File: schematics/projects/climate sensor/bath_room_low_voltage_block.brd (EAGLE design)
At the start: 100 x 80 mm, 8 parts

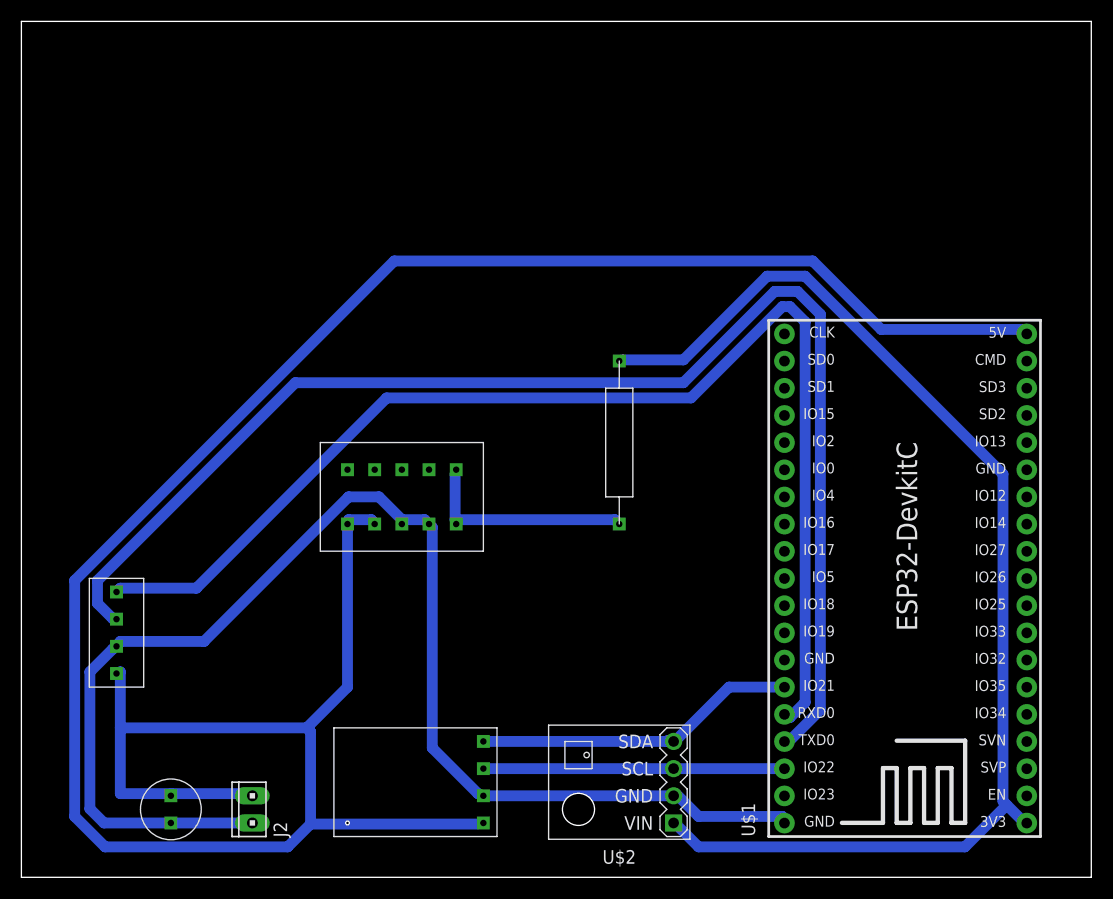
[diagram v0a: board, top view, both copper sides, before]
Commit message: added eagle board files for low-voltage schemas
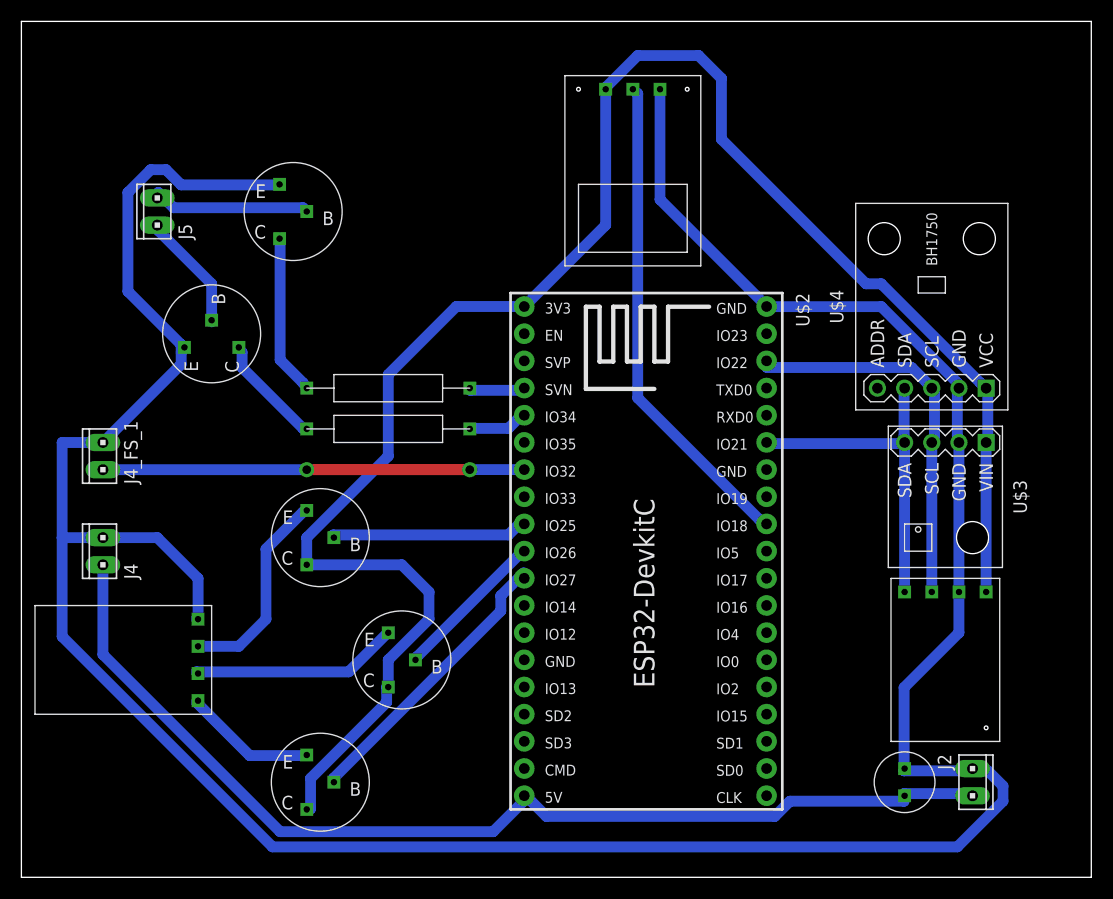
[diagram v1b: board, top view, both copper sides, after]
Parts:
- removed GY_SGP1: GY-SGP30, my_devices:GY-SGP30
- removed R1: 600, my_devices:R
- removed U$1: ESP32DEVKITC, ESP32-DEVKITC:ESP32-DEVKITC
- removed U$11: MH_Z19B, my_devices:MH_Z19B
- added GY_SGP30_1: GY-SGP30, my_devices:GY-SGP30
- added J4, J4_FS_1, J5: (no value), con-amp:10X02MTA
- added Q1, Q2, Q3, Q4, Q5: KT3102BM, my_devices:TRANSISTOR_NPN
- added R2, R3: 600, my_devices:R
- added U$4: LIGHT-SENSOR-BH1750, diy-modules:LIGHT-SENSOR-BH1750
- added U$5: TTP223, my_devices:TTP223
- added U$6: RGBLED, my_devices:RGBLED
- U$2: value TEMP-HUM-PRES-BME280 -> ESP32DEVKITC; device diy-modules:TEMP-HUM-PRES-BME280 -> ESP32-DEVKITC:ESP32-DEVKITC
- U$3: value PMS7003 -> TEMP-HUM-PRES-BME280; device my_devices:PMS7003 -> diy-modules:TEMP-HUM-PRES-BME280
- moved C1 68.6 mm to (82.5, 8.89), turned to 90 degrees
- moved J2 67.4 mm to (88.9, 8.89), turned to 270 degrees
- moved U$3 50.8 mm to (86.4, 35.6), turned to 270 degrees
- moved U$2 21.7 mm to (58.4, 30.5), turned to 270 degrees
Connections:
- removed net UART_0_RXD: U$1.34, U$11.TX
- removed net UART_0_TXD: U$1.35, U$11.RX
- removed net UART_1_RXD: U$3.TXD
- removed net UART_1_TXD: U$3.RXD
- new net GPIO_AN_A: R2.P$2, U$2.4
- new net GPIO_AN_B: R3.P$2, U$2.5
- new net GPIO_RGB_B: Q3.B, U$2.11
- new net GPIO_RGB_G: Q2.B, U$2.10
- new net GPIO_RGB_R: Q1.B, U$2.9
- new net GPIO_TTP223: U$2.30, U$5.OUT
- new net N$1: J4_FS_1.2, U$2.7
- new net N$2: Q3.E, U$6.VIN_B
- new net N$3: Q2.E, U$6.VIN_G
- new net N$4: Q1.E, U$6.VIN_R
- new net N$5: J5.1, Q5.B
- new net N$6: J5.2, Q4.B
- new net N$7: Q5.C, R2.P$1
- net +5V: now also J4.2, U$2.19; no longer U$1.19, U$11.VCC, U$3.VIN, U$3.VIN_1
- net 3V3: now also GY_SGP30_1.VIN, Q1.C, Q2.C, Q3.C, U$3.1, U$4.1, U$5.VIN; no longer GY_SGP1.VIN, R1.P$1, U$1.1
- net GND: now also GY_SGP30_1.GND, J4.1, J4_FS_1.1, Q4.E, Q5.E, U$2.38, U$3.2, U$4.2, U$5.GND, U$6.GND; no longer GY_SGP1.GND, U$1.38, U$11.GND, U$2.2, U$3.GND, U$3.GND_1
- net I2C_SCL: now also GY_SGP30_1.SCL, U$2.36, U$3.3, U$4.3; no longer GY_SGP1.SCL, U$1.36, U$2.3
- net I2C_SDA: now also GY_SGP30_1.SDA, U$2.33, U$3.4, U$4.4; no longer GY_SGP1.SDA, U$1.33, U$2.4
- net N$8: now also Q4.C, R3.P$1; no longer R1.P$2, U$3.RESET, U$3.SET
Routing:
- net GND: track 125.7 -> 278.8 mm
- net +5V: track 241.8 -> 100.4 mm
- net UART_0_TXD: track 125.7 -> 0.00 mm
- net UART_0_RXD: track 114.2 -> 0.00 mm
- net 3V3: track 114.2 -> 170.0 mm
- net GPIO_TTP223: track 0.00 -> 45.9 mm
- net N$1: track 0.00 -> 39.4 mm, vias 0 -> 2
- net GPIO_RGB_B: track 0.00 -> 27.4 mm
- net N$3: track 0.00 -> 19.7 mm
- net N$4: track 0.00 -> 19.2 mm
- net GPIO_RGB_R: track 0.00 -> 19.0 mm
- net N$5: track 0.00 -> 15.1 mm
- net N$7: track 0.00 -> 15.1 mm
- net GPIO_RGB_G: track 0.00 -> 14.5 mm
- net N$2: track 0.00 -> 12.6 mm
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
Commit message: changes in board files.
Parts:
- moved Q5 1.27 mm to (25.4, 63.5)
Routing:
- net GND: track 278.8 -> 303.3 mm
- net +5V: track 100.4 -> 102.3 mm
- net N$7: track 15.1 -> 16.4 mm
- net N$5: track 15.1 -> 14.0 mm
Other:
- board text added: "A B"
- board text added: "AN_OUT"
- board text added: "AN_POWER"
- board text added: "FS"
- board text added: "GND +5V"
- board text added: "GND 3V3"
- board text added: "SUPPLY"
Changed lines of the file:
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@@
 <wire x1="100" y1="80" x2="0" y2="80" width="0" layer="20"/>
 <wire x1="0" y1="80" x2="0" y2="0" width="0" layer="20"/>
+<text x="83.82" y="2.54" size="1.778" layer="1">SUPPLY</text>
+<text x="6.35" y="34.29" size="1.778" layer="1">AN_POWER</text>
+<text x="7.62" y="66.04" size="1.778" layer="1">AN_OUT</text>
+<text x="6.35" y="59.69" size="1.778" layer="1">A
+B</text>
+<text x="11.43" y="27.94" size="1.778" layer="1">GND
++5V</text>
+<text x="92.71" y="6.35" size="1.778" layer="1">GND
++5V</text>
+<text x="6.35" y="43.18" size="1.778" layer="1">FS</text>
+<text x="11.43" y="36.83" size="1.778" layer="1">GND
+3V3</text>
 </plain>
 <attributes>
@@
 <element name="Q3" library="my_devices" package="TRANSISTOR_NPN" value="KT3102BM" x="27.94" y="8.89" smashed="yes" rot="R180"/>
 <element name="Q4" library="my_devices" package="TRANSISTOR_NPN" value="KT3102BM" x="17.78" y="50.8" smashed="yes" rot="R270"/>
-<element name="Q5" library="my_devices" package="TRANSISTOR_NPN" value="KT3102BM" x="25.4" y="62.23" smashed="yes" rot="R180"/>
+<element name="Q5" library="my_devices" package="TRANSISTOR_NPN" value="KT3102BM" x="25.4" y="63.5" smashed="yes" rot="R180"/>
 <element name="R2" library="my_devices" package="R" value="600" x="34.29" y="45.72" smashed="yes">
 <attribute name="R" value="" x="68.58" y="-31.75" size="1.778" layer="27" display="off"/>
@@
 <contactref element="Q4" pad="E"/>
 <wire x1="16.3576" y1="24.1808" x2="16.51" y2="24.13" width="1.016" layer="16"/>
-<wire x1="14.9352" y1="49.0728" x2="15.24" y2="49.53" width="1.016" layer="16"/>
-<wire x1="14.9352" y1="64.7192" x2="24.1808" y2="64.7192" width="1.016" layer="16"/>
-<wire x1="13.5128" y1="66.1416" x2="14.9352" y2="64.7192" width="1.016" layer="16"/>
-<wire x1="12.0904" y1="66.1416" x2="13.5128" y2="66.1416" width="1.016" layer="16"/>
-<wire x1="9.9568" y1="64.008" x2="12.0904" y2="66.1416" width="1.016" layer="16"/>
-<wire x1="9.9568" y1="54.7624" x2="9.9568" y2="64.008" width="1.016" layer="16"/>
-<wire x1="14.9352" y1="49.784" x2="9.9568" y2="54.7624" width="1.016" layer="16"/>
-<wire x1="24.1808" y1="64.7192" x2="24.13" y2="64.77" width="1.016" layer="16"/>
-<wire x1="14.9352" y1="49.784" x2="15.24" y2="49.53" width="1.016" layer="16"/>
+<wire x1="24.1808" y1="65.9892" x2="24.13" y2="66.04" width="1.016" layer="16"/>
 <wire x1="88.9" y1="9.9568" x2="82.4992" y2="9.9568" width="1.016" layer="16"/>
 <wire x1="82.4992" y1="9.9568" x2="82.55" y2="10.16" width="1.016" layer="16"/>
@@
 <wire x1="69.6976" y1="53.34" x2="69.65" y2="53.35" width="1.016" layer="16"/>
 <wire x1="87.4776" y1="46.228" x2="87.63" y2="45.72" width="1.016" layer="16"/>
-<wire x1="87.4776" y1="2.8448" x2="23.4696" y2="2.8448" width="1.016" layer="16"/>
-<wire x1="91.7448" y1="7.112" x2="87.4776" y2="2.8448" width="1.016" layer="16"/>
-<wire x1="91.7448" y1="8.5344" x2="91.7448" y2="7.112" width="1.016" layer="16"/>
-<wire x1="90.3224" y1="9.9568" x2="91.7448" y2="8.5344" width="1.016" layer="16"/>
-<wire x1="88.9" y1="9.9568" x2="90.3224" y2="9.9568" width="1.016" layer="16"/>
 <wire x1="88.9" y1="9.9568" x2="88.9" y2="10.16" width="1.016" layer="16"/>
 <wire x1="87.63" y1="40.64" x2="87.63" y2="26.67" width="1.016" layer="16"/>
 <wire x1="87.63" y1="26.67" x2="87.63" y2="22.86" width="1.016" layer="16"/>
 <wire x1="82.4992" y1="17.7292" x2="82.4992" y2="9.9568" width="1.016" layer="16"/>
-<wire x1="87.63" y1="22.86" x2="82.4992" y2="17.7292" width="1.016" layer="16"/>
+<wire x1="82.4992" y1="17.7292" x2="87.63" y2="22.86" width="1.016" layer="16"/>
 <wire x1="59.69" y1="73.66" x2="59.69" y2="63.3476" width="1.016" layer="16"/>
 <wire x1="59.69" y1="63.3476" x2="69.6976" y2="53.34" width="1.016" layer="16"/>
@@
 <wire x1="3.81" y1="31.75" x2="3.81" y2="40.64" width="1.016" layer="16"/>
 <wire x1="3.81" y1="40.64" x2="7.62" y2="40.64" width="1.016" layer="16"/>
-<wire x1="7.62" y1="40.64" x2="14.9352" y2="47.9552" width="1.016" layer="16"/>
-<wire x1="14.9352" y1="47.9552" x2="14.9352" y2="49.784" width="1.016" layer="16"/>
 <contactref element="J4" pad="1"/>
 <wire x1="3.81" y1="31.75" x2="7.62" y2="31.75" width="1.016" layer="16"/>
@@
 <wire x1="16.51" y1="24.3332" x2="16.3576" y2="24.1808" width="1.016" layer="16"/>
 <wire x1="7.62" y1="31.75" x2="12.7" y2="31.75" width="1.016" layer="16"/>
+<wire x1="87.63" y1="22.86" x2="95.25" y2="15.24" width="1.016" layer="16"/>
+<wire x1="95.25" y1="5.08" x2="93.0148" y2="2.8448" width="1.016" layer="16"/>
+<wire x1="93.0148" y1="2.8448" x2="23.4696" y2="2.8448" width="1.016" layer="16"/>
+<wire x1="95.25" y1="15.24" x2="95.25" y2="5.08" width="1.016" layer="16"/>
+<wire x1="7.62" y1="40.64" x2="7.62" y2="49.53" width="1.016" layer="16"/>
+<wire x1="7.62" y1="49.53" x2="7.62" y2="64.77" width="1.016" layer="16"/>
+<wire x1="7.62" y1="64.77" x2="11.43" y2="68.58" width="1.016" layer="16"/>
+<wire x1="21.59" y1="68.58" x2="24.13" y2="66.04" width="1.016" layer="16"/>
+<wire x1="11.43" y1="68.58" x2="21.59" y2="68.58" width="1.016" layer="16"/>
+<wire x1="7.62" y1="49.53" x2="15.24" y2="49.53" width="1.016" layer="16"/>
 </signal>
 <signal name="I2C_SCL">
@@
 <wire x1="82.4992" y1="7.8232" x2="82.55" y2="7.62" width="1.016" layer="16"/>
 <wire x1="88.9" y1="7.8232" x2="88.9" y2="7.62" width="1.016" layer="16"/>
-<wire x1="44.0944" y1="4.2672" x2="24.1808" y2="4.2672" width="1.016" layer="16"/>
-<wire x1="46.9392" y1="7.112" x2="44.0944" y2="4.2672" width="1.016" layer="16"/>
 <wire x1="46.9392" y1="7.112" x2="47" y2="7.63" width="1.016" layer="16"/>
-<wire x1="71.8312" y1="7.112" x2="82.4992" y2="7.112" width="1.016" layer="16"/>
-<wire x1="70.4088" y1="5.6896" x2="71.8312" y2="7.112" width="1.016" layer="16"/>
-<wire x1="49.0728" y1="5.6896" x2="70.4088" y2="5.6896" width="1.016" layer="16"/>
-<wire x1="47.6504" y1="7.112" x2="49.0728" y2="5.6896" width="1.016" layer="16"/>
-<wire x1="82.4992" y1="7.112" x2="82.55" y2="7.62" width="1.016" layer="16"/>
-<wire x1="47.6504" y1="7.112" x2="47" y2="7.63" width="1.016" layer="16"/>
-<wire x1="7.62" y1="20.828" x2="24.1808" y2="4.2672" width="1.016" layer="16"/>
+<wire x1="24.1808" y1="4.2672" x2="7.62" y2="20.828" width="1.016" layer="16"/>
 <contactref element="J4" pad="2"/>
 <wire x1="7.62" y1="29.21" x2="7.62" y2="20.828" width="1.016" layer="16"/>
+<wire x1="82.55" y1="7.62" x2="79.1972" y2="4.2672" width="1.016" layer="16"/>
+<wire x1="79.1972" y1="4.2672" x2="46.99" y2="4.2672" width="1.016" layer="16"/>
+<wire x1="46.99" y1="4.2672" x2="24.1808" y2="4.2672" width="1.016" layer="16"/>
+<wire x1="47" y1="7.63" x2="46.99" y2="7.62" width="1.016" layer="16"/>
+<wire x1="46.99" y1="7.62" x2="46.99" y2="4.2672" width="1.016" layer="16"/>
 </signal>
 <signal name="3V3">
@@
 <wire x1="34.1376" y1="17.78" x2="34.29" y2="17.78" width="1.016" layer="16"/>
 <wire x1="46.9392" y1="53.34" x2="47" y2="53.35" width="1.016" layer="16"/>
-<wire x1="80.3656" y1="55.4736" x2="89.6112" y2="46.228" width="1.016" layer="16"/>
-<wire x1="78.9432" y1="55.4736" x2="80.3656" y2="55.4736" width="1.016" layer="16"/>
-<wire x1="65.4304" y1="68.9864" x2="78.9432" y2="55.4736" width="1.016" layer="16"/>
-<wire x1="65.4304" y1="74.676" x2="65.4304" y2="68.9864" width="1.016" layer="16"/>
-<wire x1="63.2968" y1="76.8096" x2="65.4304" y2="74.676" width="1.016" layer="16"/>
+<wire x1="65.4304" y1="74.676" x2="63.2968" y2="76.8096" width="1.016" layer="16"/>
 <wire x1="63.2968" y1="76.8096" x2="57.6072" y2="76.8096" width="1.016" layer="16"/>
 <wire x1="89.6112" y1="46.228" x2="90.17" y2="45.72" width="1.016" layer="16"/>
@@
 <wire x1="26.67" y1="31.75" x2="34.29" y2="39.37" width="1.016" layer="16"/>
 <wire x1="34.29" y1="46.99" x2="40.65" y2="53.35" width="1.016" layer="16"/>
+<wire x1="65.4304" y1="70.4088" x2="65.4304" y2="74.676" width="1.016" layer="16"/>
+<wire x1="90.17" y1="45.72" x2="90.1192" y2="45.72" width="1.016" layer="16"/>
+<wire x1="90.1192" y1="45.72" x2="65.4304" y2="70.4088" width="1.016" layer="16"/>
 </signal>
 <signal name="GPIO_TTP223">
@@
 <contactref element="J5" pad="1"/>
 <contactref element="Q5" pad="B"/>
-<wire x1="14.224" y1="62.5856" x2="26.3144" y2="62.5856" width="1.016" layer="16"/>
-<wire x1="12.8016" y1="64.008" x2="14.224" y2="62.5856" width="1.016" layer="16"/>
-<wire x1="26.3144" y1="62.5856" x2="26.67" y2="62.23" width="1.016" layer="16"/>
-<wire x1="12.8016" y1="64.008" x2="12.7" y2="63.5" width="1.016" layer="16"/>
+<wire x1="12.7" y1="63.5" x2="26.67" y2="63.5" width="1.016" layer="16"/>
 </signal>
 <signal name="N$6">
@@
 <contactref element="Q5" pad="C"/>
 <contactref element="R2" pad="P$1"/>
-<wire x1="24.1808" y1="48.3616" x2="24.1808" y2="59.7408" width="1.016" layer="16"/>
+<wire x1="24.1808" y1="48.3616" x2="24.1808" y2="61.0108" width="1.016" layer="16"/>
 <wire x1="26.3144" y1="46.228" x2="24.1808" y2="48.3616" width="1.016" layer="16"/>
-<wire x1="24.1808" y1="59.7408" x2="24.13" y2="59.69" width="1.016" layer="16"/>
+<wire x1="24.1808" y1="61.0108" x2="24.13" y2="60.96" width="1.016" layer="16"/>
 <wire x1="26.3144" y1="46.228" x2="26.67" y2="45.72" width="1.016" layer="16"/>
 </signal>
@@
 </drawing>
 <compatibility>
+<note version="6.3" minversion="6.2.2" severity="warning">
+Since Version 6.2.2 text objects can contain more than one line,
+which will not be processed correctly with this version.
+</note>
 <note version="8.2" severity="warning">
 Since Version 8.2, EAGLE supports online libraries. The ids

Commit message: actualized schematics
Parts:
- moved Q2 8.03 mm to (27.9, 22.9)
- moved R3 5.08 mm to (34.3, 47.0)
- moved Q3 5.08 mm to (27.9, 14.0)
- moved U$3 5.08 mm to (86.4, 40.6)
- moved U$4 5.08 mm to (85.1, 58.4)
- moved R2 3.81 mm to (34.3, 49.5)
- moved GY_SGP30_1 3.81 mm to (86.4, 30.5)
- moved C1 2.54 mm to (80.0, 8.89)
- moved Q5 1.27 mm to (25.4, 64.8)
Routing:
- net GND: track 303.3 -> 315.6 mm
- net GPIO_RGB_G: track 14.5 -> 24.0 mm
- net 3V3: track 170.0 -> 178.2 mm, vias 0 -> 4
- net N$3: track 19.7 -> 14.0 mm
- net GPIO_RGB_B: track 27.4 -> 31.9 mm
- net I2C_SCL: track 36.3 -> 40.4 mm
- net GPIO_AN_A: track 5.41 -> 8.90 mm
- net GPIO_AN_B: track 5.84 -> 8.90 mm
- net N$6: track 11.1 -> 14.0 mm
- net N$5: track 14.0 -> 11.4 mm
- net GPIO_RGB_R: track 19.0 -> 21.4 mm
- net N$2: track 12.6 -> 10.9 mm
- net N$4: track 19.2 -> 17.9 mm
- net +5V: track 102.3 -> 103.5 mm
- net I2C_SDA: track 32.1 -> 33.2 mm
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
